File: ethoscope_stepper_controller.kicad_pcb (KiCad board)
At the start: 2 copper layers, 121.3 x 67.3 mm, 1 part

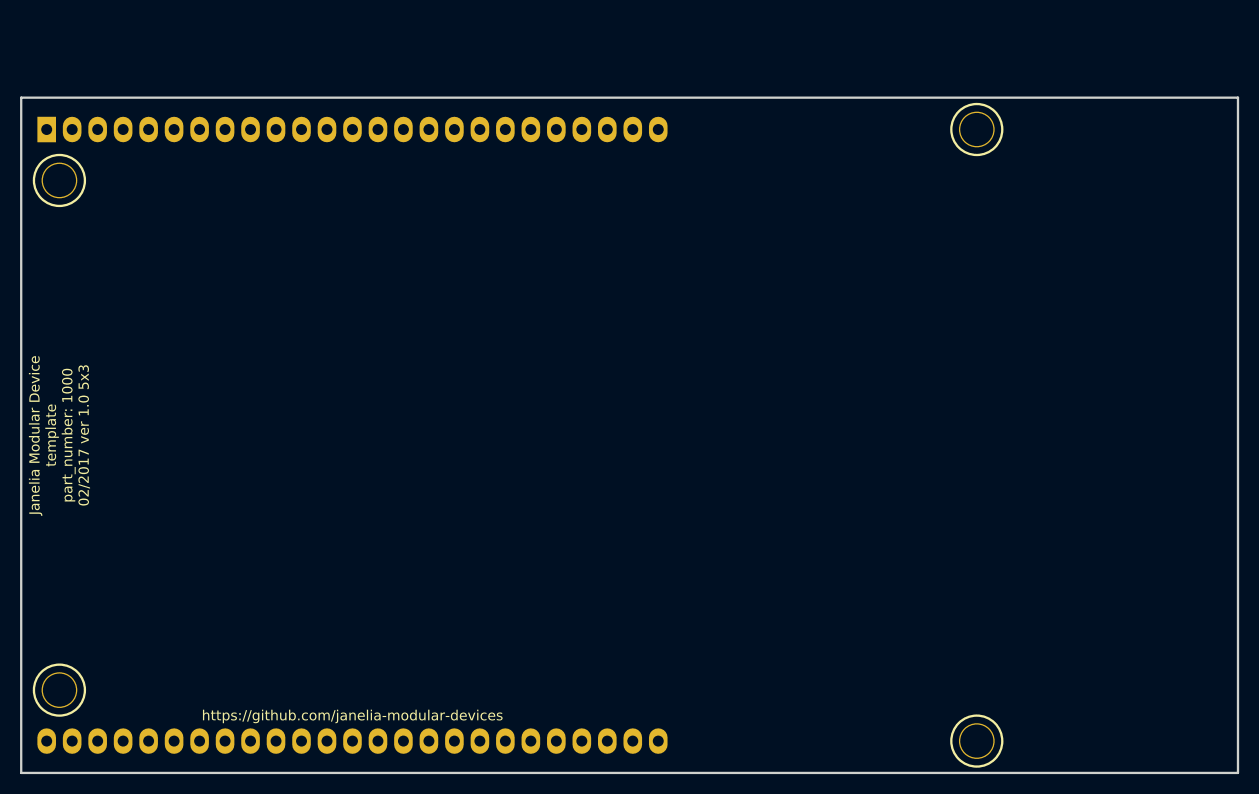
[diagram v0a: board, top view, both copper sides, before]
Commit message: Added files from step_dir_controller.
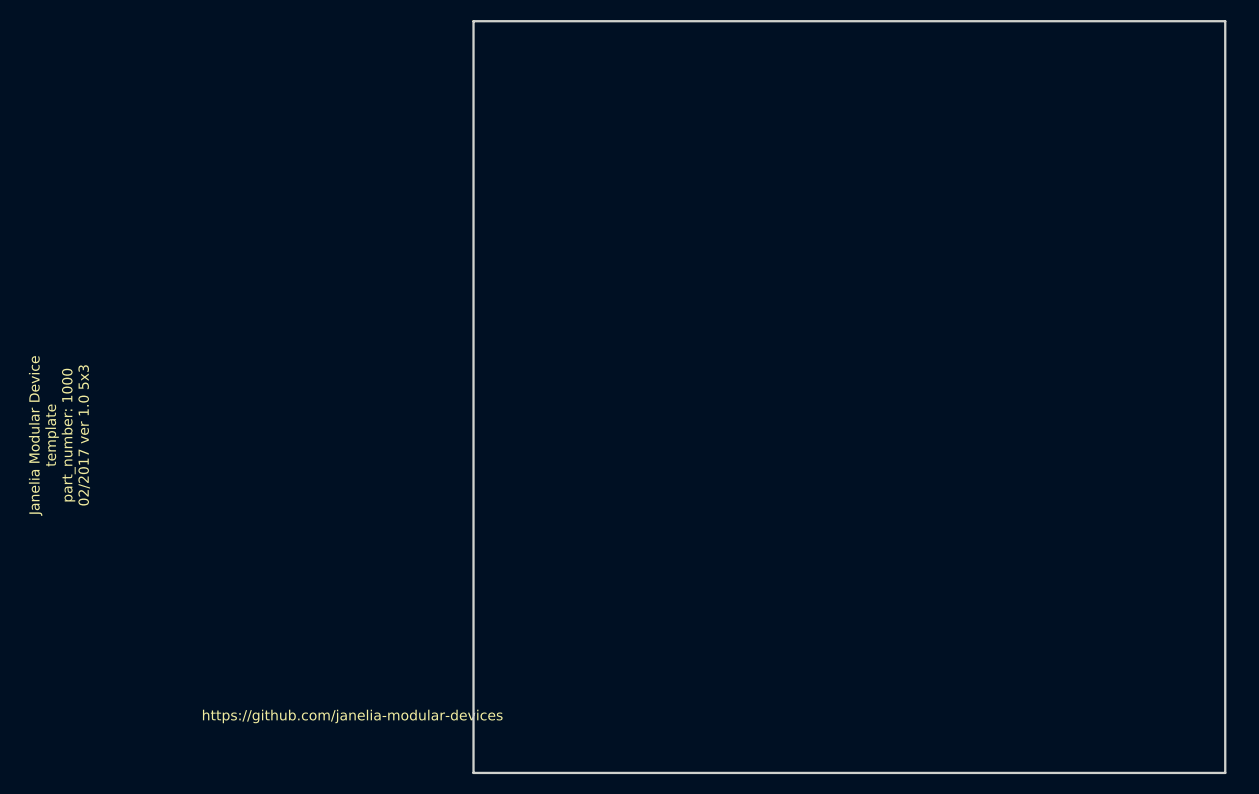
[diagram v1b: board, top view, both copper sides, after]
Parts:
- removed MDB1: MODULAR_DEVICE_BASE_5x3_MALE, ethoscope_stepper_controller:MODULAR_DEVICE_BASE_5X3_MALE
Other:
- board size 121.3 x 67.3 mm -> 74.9 x 74.9 mm

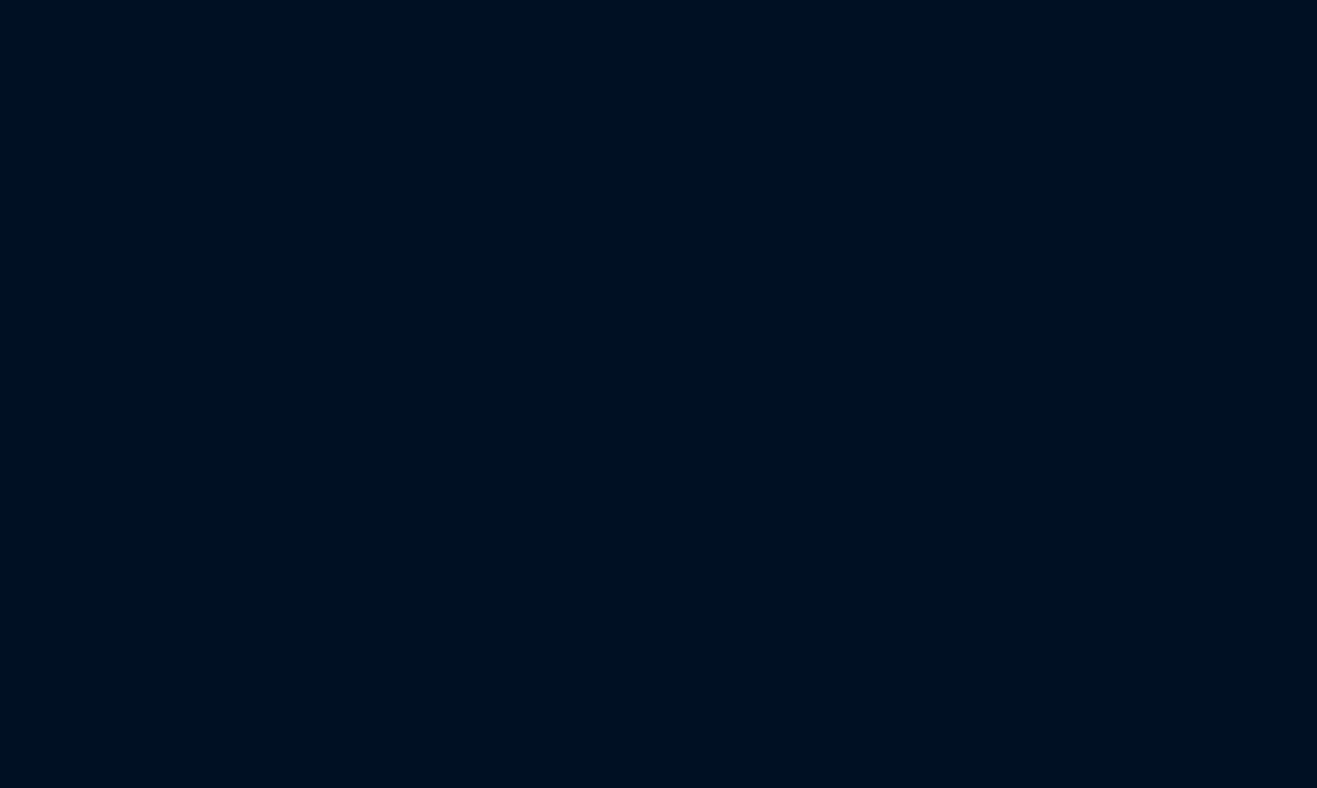
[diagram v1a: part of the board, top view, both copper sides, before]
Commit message: Fixed footprints.
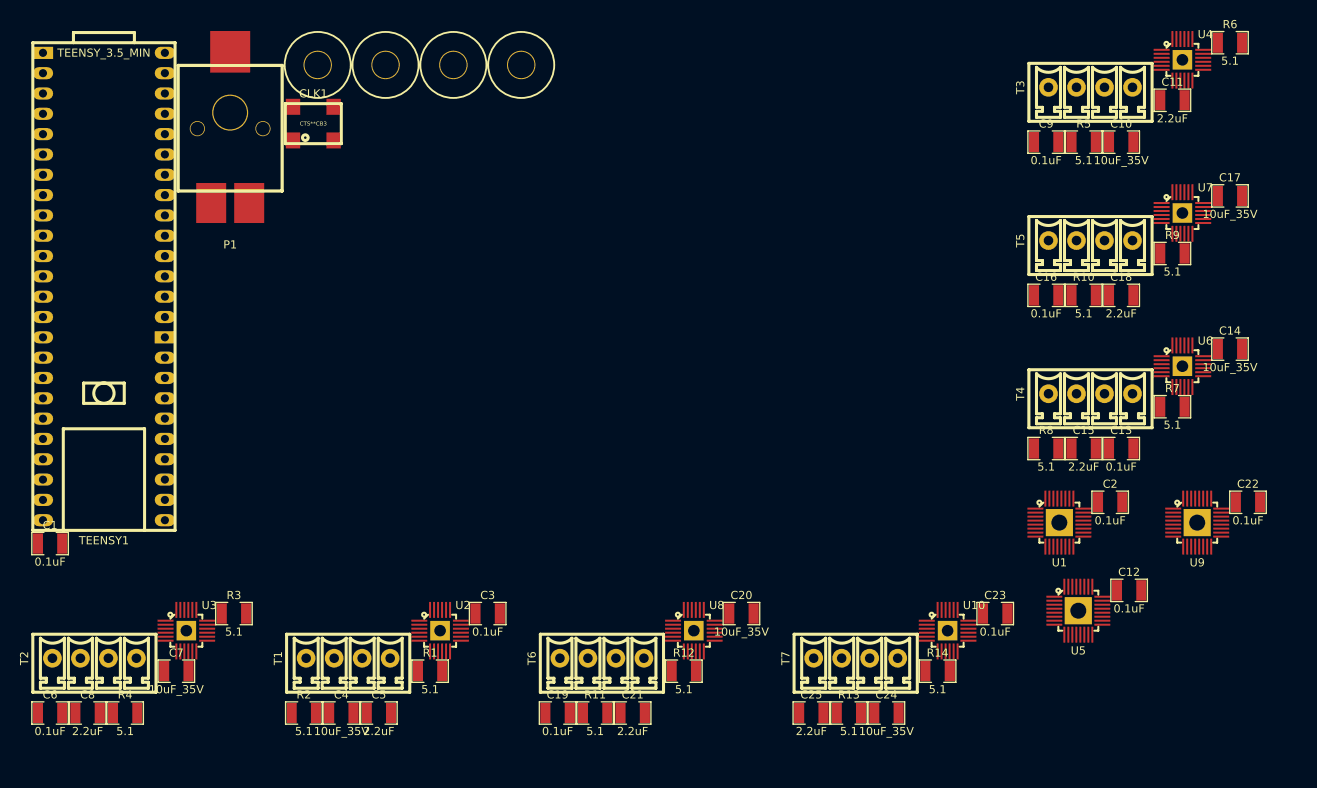
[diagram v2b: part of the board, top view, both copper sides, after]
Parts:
- added C1: 0.1uF, ethoscope_stepper_controller:SM1210, F.Cu at (-58.6, 26.0)
- added C10: 10uF_35V, footprints:SM1210, F.Cu at (75.3, -24.2)
- added C11: 2.2uF, footprints:SM1210, F.Cu at (81.7, -29.4)
- added C12: 0.1uF, ethoscope_stepper_controller:SM1210, F.Cu at (76.3, 31.8)
- added C13: 0.1uF, ethoscope_stepper_controller:SM1210, F.Cu at (75.3, 14.1)
- added C14: 10uF_35V, footprints:SM1210, F.Cu at (88.9, 1.66)
- added C15: 2.2uF, footprints:SM1210, F.Cu at (70.6, 14.1)
- added C16: 0.1uF, ethoscope_stepper_controller:SM1210, F.Cu at (65.9, -5.06)
- added C17: 10uF_35V, footprints:SM1210, F.Cu at (88.9, -17.5)
- added C18: 2.2uF, footprints:SM1210, F.Cu at (75.3, -5.06)
- added C19: 0.1uF, ethoscope_stepper_controller:SM1210, F.Cu at (4.83, 47.2)
- added C2: 0.1uF, ethoscope_stepper_controller:SM1210, F.Cu at (73.9, 20.8)
- added C20: 10uF_35V, footprints:SM1210, F.Cu at (27.8, 34.7)
- added C21: 2.2uF, footprints:SM1210, F.Cu at (14.2, 47.2)
- added C22: 0.1uF, ethoscope_stepper_controller:SM1210, F.Cu at (91.1, 20.8)
- added C23: 0.1uF, ethoscope_stepper_controller:SM1210, F.Cu at (59.5, 34.7)
- added C24: 10uF_35V, footprints:SM1210, F.Cu at (45.9, 47.2)
- added C25: 2.2uF, footprints:SM1210, F.Cu at (36.5, 47.2)
- added C3: 0.1uF, ethoscope_stepper_controller:SM1210, F.Cu at (-3.91, 34.7)
- added C4: 10uF_35V, footprints:SM1210, F.Cu at (-22.2, 47.2)
- added C5: 2.2uF, footprints:SM1210, F.Cu at (-17.5, 47.2)
- added C6: 0.1uF, ethoscope_stepper_controller:SM1210, F.Cu at (-58.6, 47.2)
- added C7: 10uF_35V, footprints:SM1210, F.Cu at (-42.8, 41.9)
- added C8: 2.2uF, footprints:SM1210, F.Cu at (-53.9, 47.2)
- added C9: 0.1uF, ethoscope_stepper_controller:SM1210, F.Cu at (65.9, -24.2)
- added CLK1: CLK_32MHZ, ethoscope_stepper_controller:CTS_SMD_4_7X5MM, F.Cu at (-25.7, -26.5)
- added MH1: MOUNT_HOLE, ethoscope_stepper_controller:MOUNTING_HOLE_4-40, F.Cu at (0.28, -33.9)
- added MH2: MOUNT_HOLE, ethoscope_stepper_controller:MOUNTING_HOLE_4-40, F.Cu at (-8.20, -33.9)
- added MH3: MOUNT_HOLE, ethoscope_stepper_controller:MOUNTING_HOLE_4-40, F.Cu at (-16.7, -33.9)
- added MH4: MOUNT_HOLE, ethoscope_stepper_controller:MOUNTING_HOLE_4-40, F.Cu at (-25.2, -33.9)
- added P1: PWR_JACK_2.1x5.5_SMD_VERT, ethoscope_stepper_controller:DCJACK_3PIN_SMD_VERT, F.Cu at (-36.1, -27.9)
- added R1: 5.1, ethoscope_stepper_controller:SM1210, F.Cu at (-11.1, 41.9)
- added R10: 5.1, ethoscope_stepper_controller:SM1210, F.Cu at (70.6, -5.06)
- added R11: 5.1, ethoscope_stepper_controller:SM1210, F.Cu at (9.52, 47.2)
- added R12: 5.1, ethoscope_stepper_controller:SM1210, F.Cu at (20.6, 41.9)
- added R13: 5.1, ethoscope_stepper_controller:SM1210, F.Cu at (41.2, 47.2)
- added R14: 5.1, ethoscope_stepper_controller:SM1210, F.Cu at (52.3, 41.9)
- added R2: 5.1, ethoscope_stepper_controller:SM1210, F.Cu at (-26.9, 47.2)
- added R3: 5.1, ethoscope_stepper_controller:SM1210, F.Cu at (-35.6, 34.7)
- added R4: 5.1, ethoscope_stepper_controller:SM1210, F.Cu at (-49.2, 47.2)
- added R5: 5.1, ethoscope_stepper_controller:SM1210, F.Cu at (70.6, -24.2)
- added R6: 5.1, ethoscope_stepper_controller:SM1210, F.Cu at (88.9, -36.6)
- added R7: 5.1, ethoscope_stepper_controller:SM1210, F.Cu at (81.7, 8.86)
- added R8: 5.1, ethoscope_stepper_controller:SM1210, F.Cu at (65.9, 14.1)
- added R9: 5.1, ethoscope_stepper_controller:SM1210, F.Cu at (81.7, -10.3)
- added T1: TERM_BLK_HDR_4POS_VERT_0.138IN, ethoscope_stepper_controller:TERM_BLK_HDR_4POS_VERT_0.138IN, F.Cu at (-21.3, 40.3)
- added T2: TERM_BLK_HDR_4POS_VERT_0.138IN, ethoscope_stepper_controller:TERM_BLK_HDR_4POS_VERT_0.138IN, F.Cu at (-53.1, 40.3)
- added T3: TERM_BLK_HDR_4POS_VERT_0.138IN, ethoscope_stepper_controller:TERM_BLK_HDR_4POS_VERT_0.138IN, F.Cu at (71.4, -31.1)
- added T4: TERM_BLK_HDR_4POS_VERT_0.138IN, ethoscope_stepper_controller:TERM_BLK_HDR_4POS_VERT_0.138IN, F.Cu at (71.4, 7.24)
- added T5: TERM_BLK_HDR_4POS_VERT_0.138IN, ethoscope_stepper_controller:TERM_BLK_HDR_4POS_VERT_0.138IN, F.Cu at (71.4, -11.9)
- added T6: TERM_BLK_HDR_4POS_VERT_0.138IN, ethoscope_stepper_controller:TERM_BLK_HDR_4POS_VERT_0.138IN, F.Cu at (10.4, 40.3)
- added T7: TERM_BLK_HDR_4POS_VERT_0.138IN, ethoscope_stepper_controller:TERM_BLK_HDR_4POS_VERT_0.138IN, F.Cu at (42.1, 40.3)
- added TEENSY1: TEENSY_3.5_MIN, ethoscope_stepper_controller:TEENSY_3.5_MIN, F.Cu at (-51.9, -18.9)
- added U1: TMC429, ethoscope_stepper_controller:QFN-5x5-32, F.Cu at (67.5, 23.4)
- added U10: DRV8846, ethoscope_stepper_controller:VQFN-4x4-24, F.Cu at (53.6, 36.9)
- added U2: DRV8846, ethoscope_stepper_controller:VQFN-4x4-24, F.Cu at (-9.86, 36.9)
- added U3: DRV8846, ethoscope_stepper_controller:VQFN-4x4-24, F.Cu at (-41.6, 36.9)
- added U4: DRV8846, ethoscope_stepper_controller:VQFN-4x4-24, F.Cu at (82.9, -34.5)
- added U5: TMC429, ethoscope_stepper_controller:QFN-5x5-32, F.Cu at (69.9, 34.4)
- added U6: DRV8846, ethoscope_stepper_controller:VQFN-4x4-24, F.Cu at (82.9, 3.80)
- added U7: DRV8846, ethoscope_stepper_controller:VQFN-4x4-24, F.Cu at (82.9, -15.3)
- added U8: DRV8846, ethoscope_stepper_controller:VQFN-4x4-24, F.Cu at (21.9, 36.9)
- added U9: TMC429, ethoscope_stepper_controller:QFN-5x5-32, F.Cu at (84.8, 23.4)

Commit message: Initial layout.
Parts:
- T1, T2, T3, T4, T5, T6, T7: moved to B.Cu
- moved P1 253.8 mm to (164.5, 127.6), turned to 180 degrees
- moved C6 249.5 mm to (188.0, 85.1), turned to 270 degrees
- moved MH1 241.8 mm to (179.4, 128.6)
- moved C8 241.0 mm to (184.8, 80.0), turned to 90 degrees
- moved C7 231.7 mm to (184.8, 85.1), turned to 270 degrees
- moved MH4 231.5 mm to (179.4, 74.6)
- moved TEENSY1 229.7 mm to (139.7, 108.0), turned to 180 degrees
- moved U3 225.3 mm to (179.1, 82.5)
- moved R4 225.1 mm to (172.7, 84.5), turned to 180 degrees
- moved T2 224.3 mm to (168.9, 72.4), turned to 270 degrees
- moved R3 213.4 mm to (172.7, 80.6), turned to 180 degrees
- moved MH2 210.3 mm to (125.4, 128.6)
- moved C1 208.4 mm to (127.0, 120.7), turned to 90 degrees
- moved CLK1 207.6 mm to (120.7, 120.7), turned to 90 degrees
- moved C19 192.2 mm to (188.0, 105.4), turned to 270 degrees
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
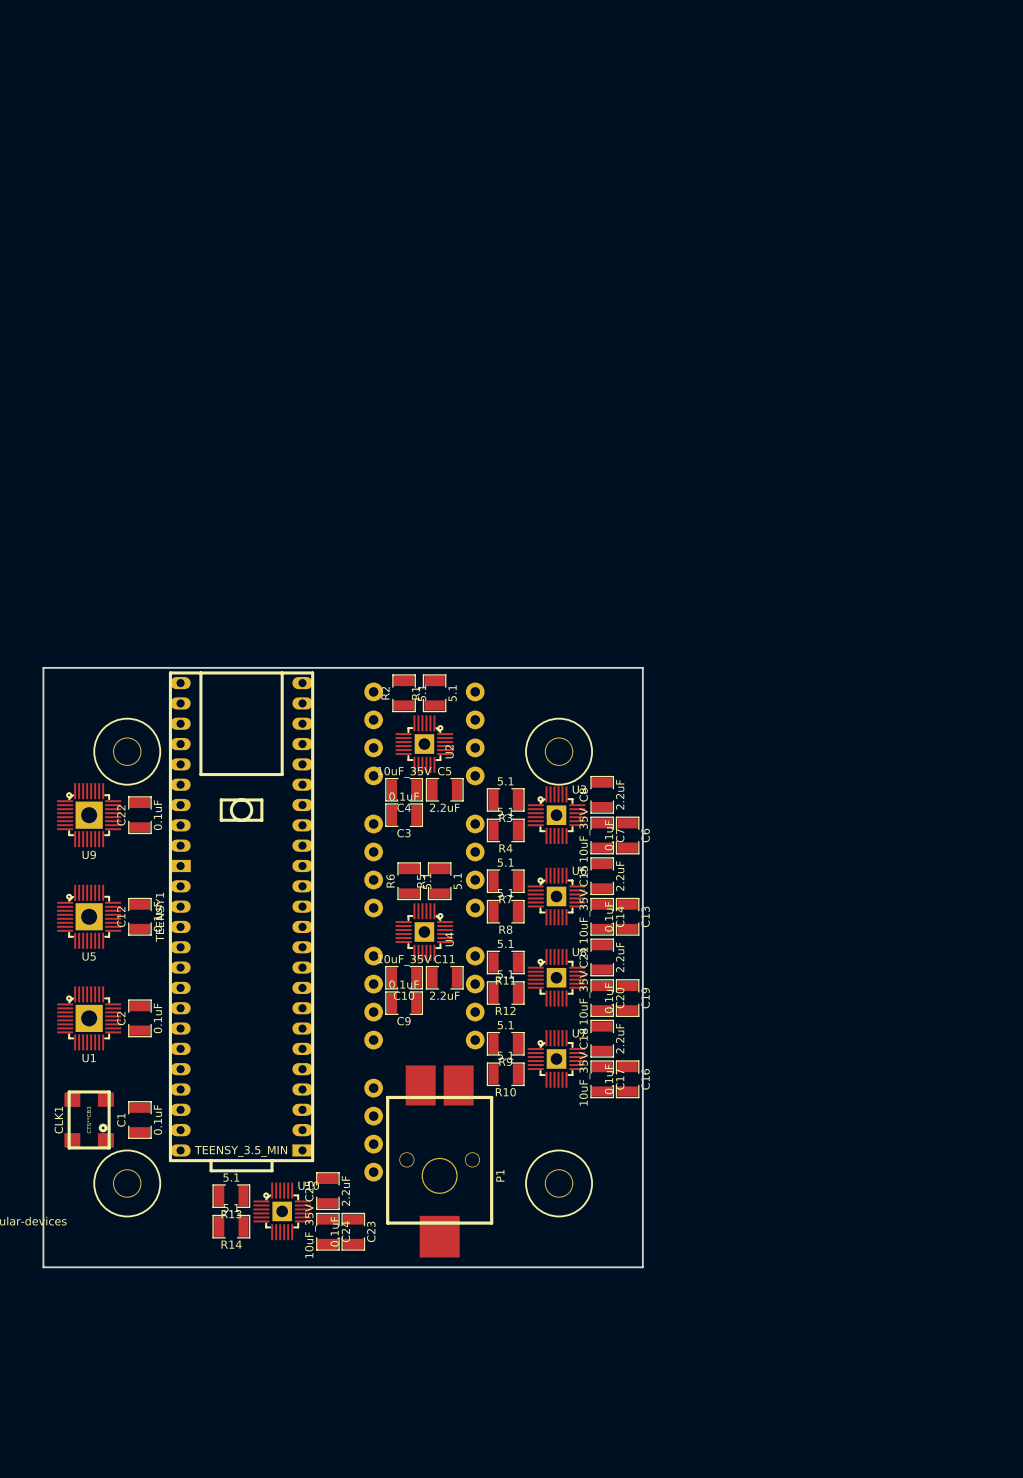
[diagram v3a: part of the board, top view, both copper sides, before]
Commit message: Switched to 0805 parts.
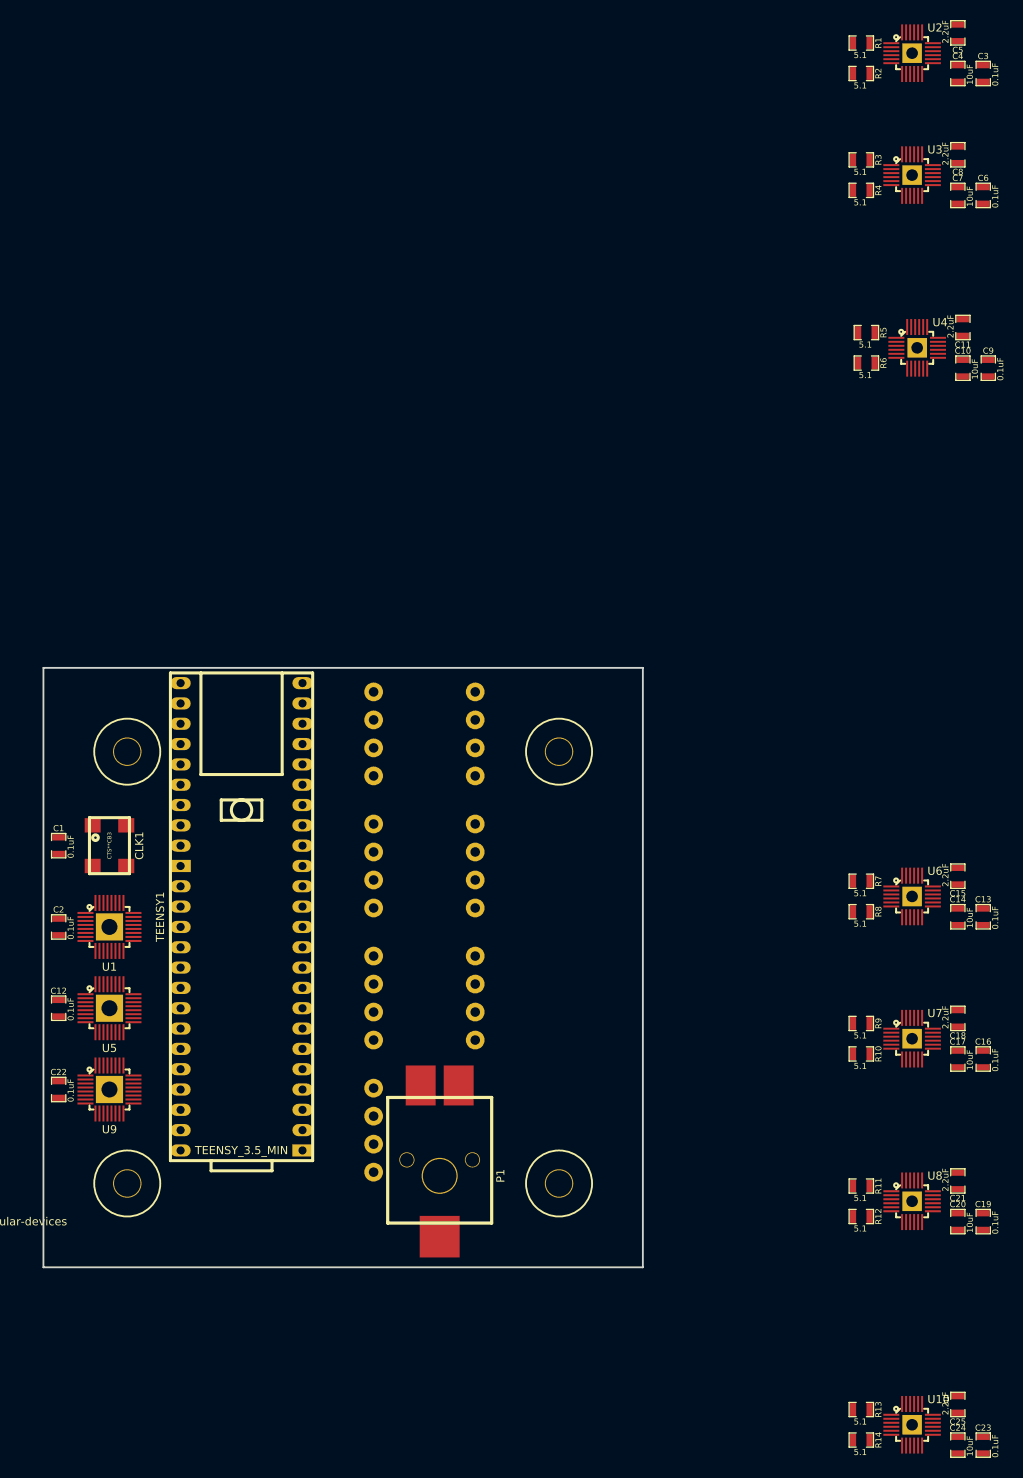
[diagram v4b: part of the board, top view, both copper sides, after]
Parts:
- C1, C12, C13, C16, C19, C2, C22, C23, C3, C6, C9: footprint ethoscope_stepper_controller:SM1210 -> ethoscope_stepper_controller:SM0805
- C10, C14, C17, C20, C24, C4, C7: value 10uF_35V -> 10uF; footprint footprints:SM1210 -> footprints:SM0805
- C11, C15, C18, C21, C25, C5, C8: footprint footprints:SM1210 -> footprints:SM0805
- R1, R10, R11, R12, R13, R14, R2, R3, R4, R5, R6, R7, R8, R9: footprint ethoscope_stepper_controller:SM1210 -> footprints:SM0805
- moved C3 117.6 mm to (232.4, -10.2), turned to 270 degrees
- moved C5 114.3 mm to (229.2, -15.2), turned to 90 degrees
- moved C4 113.2 mm to (229.2, -10.2), turned to 270 degrees
- moved C9 107.9 mm to (233.0, 26.7), turned to 270 degrees
- moved U2 105.7 mm to (223.5, -12.7), turned to 0 degrees
- moved C11 103.9 mm to (229.9, 21.6), turned to 90 degrees
- moved C10 103.4 mm to (229.9, 26.7), turned to 270 degrees
- moved R1 97.2 mm to (217.2, -14.0), turned to 180 degrees
- moved R2 96.3 mm to (217.2, -10.2), turned to 180 degrees
- moved U4 95.5 mm to (224.2, 24.1), turned to 0 degrees
- moved C7 91.5 mm to (229.2, 5.08)
- moved C8 91.5 mm to (229.2, 0.00)
- moved R3 91.5 mm to (217.2, 0.64)
- moved R4 91.5 mm to (217.2, 4.45)
- moved U3 91.5 mm to (223.5, 2.54)
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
